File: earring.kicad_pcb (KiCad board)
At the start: 2 copper layers, 41.4 x 41.9 mm, 107 parts, among them J2 USB_C_Receptacle_USB2.0, Q1 NMOS 20V 0.75A 500mΩ@4.5V, Q2 NMOS 20V 0.75A 500mΩ@4.5V, Q3 NMOS 20V 0.75A 500mΩ@4.5V, Q4 NMOS 20V 0.75A 500mΩ@4.5V, Q5 light_sensor, U1 Magnetic Switch, U10 USBLC6-2P6, U20 LGS4056H, U24 SK9822-EC20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

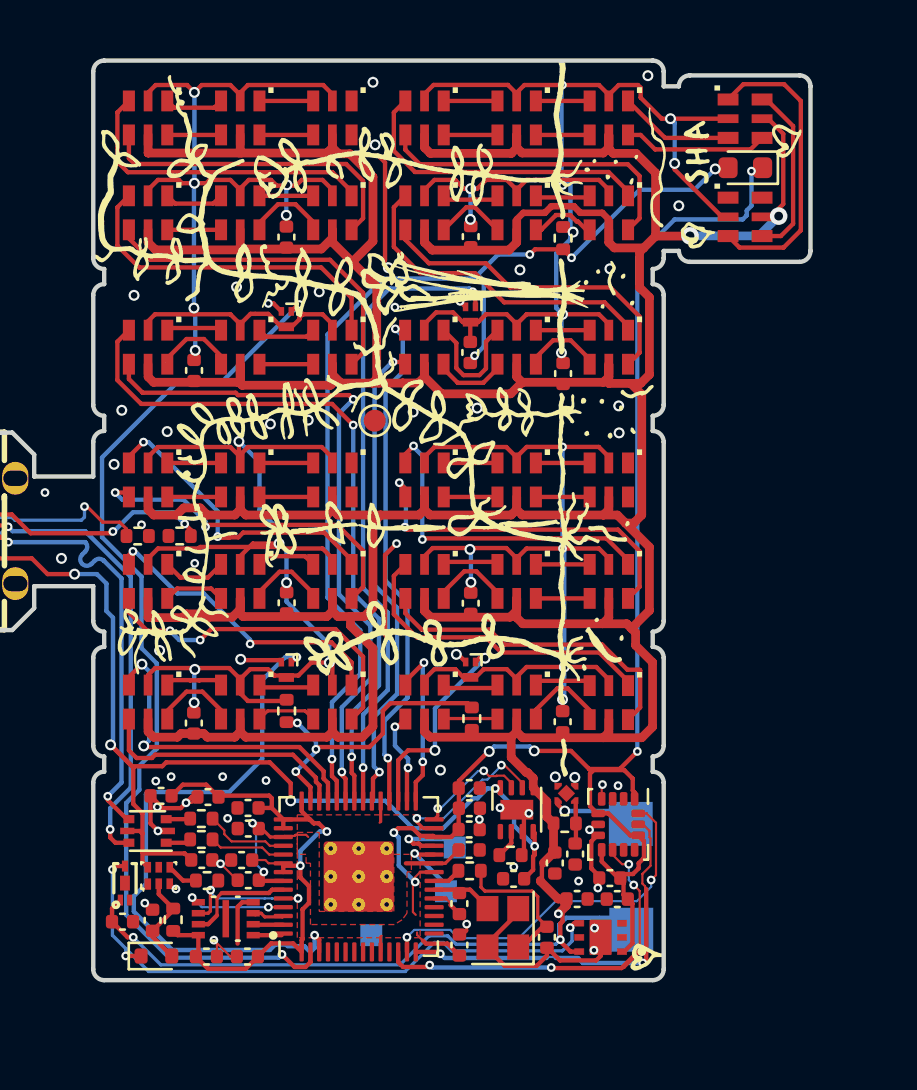
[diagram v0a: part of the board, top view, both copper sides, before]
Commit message: rework power control to simplify and remove VBAT from MCU pins
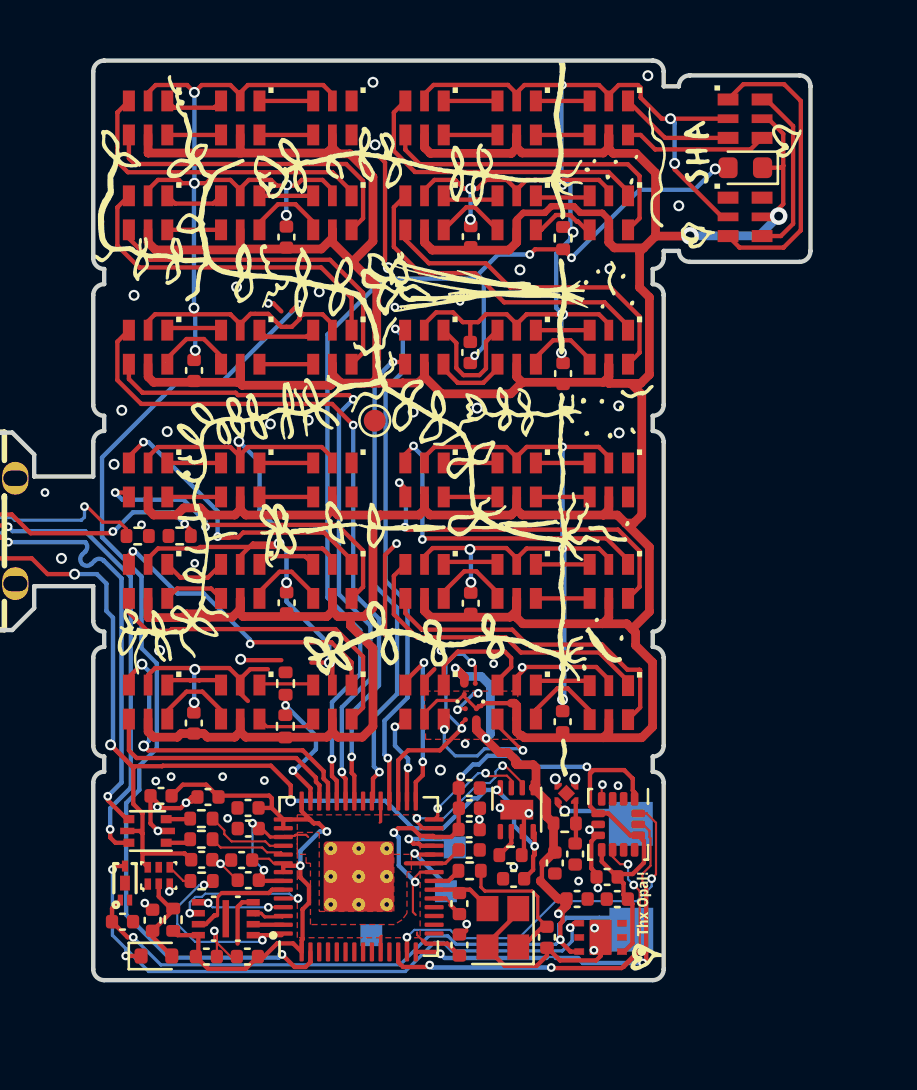
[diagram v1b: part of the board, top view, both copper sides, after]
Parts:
- removed Q1, Q2, Q3, Q4: NMOS 20V 0.75A 500mΩ@4.5V, Package_DFN_QFN:Diodes_DFN1006-3
- added U43: TPS22913BYZVR, footprints:YZV0004ADAD, F.Cu at (167.2, 92.8)
- added U44: TPS22913BYZVR, footprints:YZV0004ADAD, F.Cu at (167.2, 91.6)
- R10: value 20k -> 10k
- U4: value W25Q16JV -> W25Q16JVUXIQ
- U8: value ~ -> DS6091AED4
- moved R11 8.51 mm to (158.8, 93.4)
- moved R12 1.25 mm to (158.8, 91.4)
- moved R1 0.25 mm to (154.9, 100.4)
- moved C23 0.13 mm to (173.4, 100.2)
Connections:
- net /RUN renamed /3v3EN
- C25 pad 1: +BATT -> /LED_1_V
- C25 pad 2: /LED_4_GND -> GND
- C26 pad 1: +BATT -> /LED_1_V
- C26 pad 2: /LED_4_GND -> GND
- C27 pad 1: +BATT -> /LED_1_V
- C27 pad 2: /LED_1_GND -> GND
- C28 pad 1: +BATT -> /LED_1_V
- C28 pad 2: /LED_1_GND -> GND
- C29 pad 1: +BATT -> /LED_1_V
- C29 pad 2: /LED_3_GND -> GND
- C30 pad 1: +BATT -> /LED_1_V
- C30 pad 2: /LED_3_GND -> GND
- C31 pad 1: +BATT -> /LED_1_V
- C31 pad 2: /LED_2_GND -> GND
- C32 pad 1: +BATT -> /LED_1_V
- C32 pad 2: /LED_2_GND -> GND
- C33 pad 2: /LED_2_GND -> GND
- Q5 pad 1: +3V3 -> /LED_1_V
- R1 pad 1: /QSPI_SCLK -> /QSPI_SS
- R11 pad 2: +BATT -> /LED_1_V
- R12 pad 1: /LED_4_GND -> GND
- R8 pad 2: /LED_2_GND -> GND
- U11 pad 2: /LED_4_GND -> GND
- U11 pad 5: +BATT -> /LED_1_V
- U12 pad 2: /LED_4_GND -> GND
- U12 pad 5: +BATT -> /LED_1_V
- U13 pad 2: /LED_4_GND -> GND
- U13 pad 5: +BATT -> /LED_1_V
- U14 pad 2: /LED_4_GND -> GND
- U14 pad 5: +BATT -> /LED_1_V
- U15 pad 2: /LED_4_GND -> GND
- U15 pad 5: +BATT -> /LED_1_V
- U16 pad 2: /LED_1_GND -> GND
- U16 pad 5: +BATT -> /LED_1_V
- U17 pad 2: /LED_1_GND -> GND
- U17 pad 5: +BATT -> /LED_1_V
- U18 pad 2: /LED_1_GND -> GND
- U18 pad 5: +BATT -> /LED_1_V
- U19 pad 2: /LED_1_GND -> GND
- U19 pad 5: +BATT -> /LED_1_V
- U21 pad 2: /LED_1_GND -> GND
- U21 pad 5: +BATT -> /LED_1_V
- U22 pad 2: /LED_1_GND -> GND
- U22 pad 5: +BATT -> /LED_1_V
- U24 pad 2: /LED_3_GND -> GND
- U24 pad 5: +BATT -> /LED_1_V
- U25 pad 2: /LED_3_GND -> GND
- U25 pad 5: +BATT -> /LED_1_V
- U26 pad 2: /LED_3_GND -> GND
- U26 pad 5: +BATT -> /LED_1_V
- U27 pad 2: /LED_2_GND -> GND
- U27 pad 5: +BATT -> /LED_1_V
- U28 pad 2: /LED_2_GND -> GND
- U28 pad 5: +BATT -> /LED_1_V
- U29 pad 2: /LED_2_GND -> GND
- U29 pad 5: +BATT -> /LED_1_V
- U30 pad 2: /LED_2_GND -> GND
- U30 pad 5: +BATT -> /LED_1_V
- U31 pad 2: /LED_3_GND -> GND
- U31 pad 5: +BATT -> /LED_1_V
- U32 pad 2: /LED_3_GND -> GND
- U32 pad 5: +BATT -> /LED_1_V
- U33 pad 2: /LED_3_GND -> GND
- U33 pad 5: +BATT -> /LED_1_V
- U34 pad 2: /LED_2_GND -> GND
- U34 pad 5: +BATT -> /LED_1_V
- U35 pad 2: /LED_2_GND -> GND
- U35 pad 5: +BATT -> /LED_1_V
- U36 pad 2: /LED_2_GND -> GND
- U36 pad 5: +BATT -> /LED_1_V
- U37 pad 2: /LED_2_GND -> GND
- U37 pad 5: +BATT -> /LED_1_V
- U38 pad 2: /LED_3_GND -> GND
- U38 pad 5: +BATT -> /LED_1_V
- U39 pad 2: /LED_3_GND -> GND
- U39 pad 5: +BATT -> /LED_1_V
- U40 pad 2: /LED_3_GND -> GND
- U40 pad 5: +BATT -> /LED_1_V
- U41 pad 2: /LED_2_GND -> GND
- U41 pad 5: +BATT -> /LED_1_V
- U42 pad 2: /LED_2_GND -> GND
- U42 pad 5: +BATT -> /LED_1_V
- U45 pad 2: /LED_4_GND -> GND
- U45 pad 5: +BATT -> /LED_1_V
- U46 pad 2: /LED_4_GND -> GND
- U46 pad 5: +BATT -> /LED_1_V
- U47 pad 2: /LED_4_GND -> GND
- U47 pad 5: +BATT -> /LED_1_V
- U48 pad 2: /LED_1_GND -> GND
- U48 pad 5: +BATT -> /LED_1_V
- U49 pad 2: /LED_1_GND -> GND
- U49 pad 5: +BATT -> /LED_1_V
- U5 pad 2: /LED_4_GND -> GND
- U5 pad 5: +BATT -> /LED_1_V
- U50 pad 2: /LED_2_GND -> GND
- U50 pad 5: +BATT -> /LED_1_V
- U52 pad 2: /LED_1_GND -> GND
- U52 pad 5: +BATT -> /LED_1_V
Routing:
- net /LED_1_V: track 0.00 -> 224.6 mm, vias 0 -> 2
- net +BATT: track 266.3 -> 51.8 mm
- net GND: track 47.9 -> 242.6 mm, vias 61 -> 93
- net /LED_2_GND: track 59.8 -> 0.00 mm, vias 9 -> 0
- net /LED_4_GND: track 50.2 -> 0.00 mm, vias 6 -> 0
- net /LED_3_GND: track 46.3 -> 0.00 mm, vias 6 -> 0
- net /LED_1_GND: track 45.1 -> 0.00 mm, vias 6 -> 0
- net +3V3: track 99.1 -> 66.1 mm, vias 8 -> 6
- net /SW_LED_2: track 29.4 -> 0.00 mm, vias 2 -> 0
- net /SW_LED_4: track 28.2 -> 0.00 mm, vias 2 -> 0
- net /BATT_SENSE: track 13.7 -> 6.68 mm, vias 3 -> 2
- net /QSPI_SS: track 1.40 -> 8.06 mm, vias 0 -> 2
- net Net-(U48-CKO): track 2.47 -> 7.07 mm, vias 0 -> 2
- net Net-(U48-SDO): track 2.56 -> 6.22 mm
- net /SW_LED_1: track 9.38 -> 11.6 mm
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- added copper zone on F.Cu, net /LED_1_V
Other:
- board text added: "Thx Opal!"

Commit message: check in complex startup circuit before simplification
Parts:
- removed C24: 100n, Capacitor_SMD:C_0402_1005Metric
- removed R2: 100k, Resistor_SMD:R_0402_1005Metric
- removed U6: Buffer, digikey-footprints:UFDFN-6_1.45x1mm
- added D1: D, Diode_SMD:D_SOD-882, F.Cu at (136.0, 104.1)
- added D3: 3.3v Zener, Diode_SMD:D_SOD-882, F.Cu at (143.5, 106.0)
- added D4: D, Diode_SMD:D_SOD-882, F.Cu at (147.5, 100.6)
- added D5: D, Diode_SMD:D_SOD-882, F.Cu at (136.2, 101.3)
- added Q1: BSS214NW, Package_DFN_QFN:Diodes_DFN1006-3, F.Cu at (147.5, 102.9)
- added Q2: BSS214NW, Package_DFN_QFN:Diodes_DFN1006-3, F.Cu at (142.9, 99.4)
- added R13: 100k, Resistor_SMD:R_0402_1005Metric, F.Cu at (143.8, 101.8)
- added R15: 100k, Resistor_SMD:R_0402_1005Metric, F.Cu at (139.2, 103.9)
- added R16: 100k, Resistor_SMD:R_0402_1005Metric, F.Cu at (139.9, 99.0)
- added R17: 1M, Resistor_SMD:R_0402_1005Metric, F.Cu at (139.9, 101.0)
- added R18: 10k, Resistor_SMD:R_0402_1005Metric, F.Cu at (145.8, 105.6)
- added R20: 10k, Resistor_SMD:R_0402_1005Metric, F.Cu at (143.7, 104.4)
- D2: value D -> 3.3v Zener; footprint Diode_SMD:D_SOD-523 -> Diode_SMD:D_SOD-882
- moved C3 14.0 mm to (139.2, 105.9), turned to 0 degrees
- moved D2 7.75 mm to (147.5, 98.3)
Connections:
- C3 pad 1: Net-(D2-A) -> /~{USB_BOOT}
- C3 pad 2: GND -> Net-(Q2-D)
- D2 pad 1: /3v3EN -> /RUN
- D2 pad 2: Net-(D2-A) -> GND
- U1 pad 2: /3v3EN -> /mag
- U3 pad 2: /SW_LED_3 -> /ENA_GPIO
- U3 pad 26: +3V3 -> /RUN
- U3 pad 3: /SW_LED_4 -> /RUN
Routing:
- net /SW_LED_3: track 44.9 -> 0.00 mm, vias 2 -> 0
- net /ENA_GPIO: track 0.00 -> 44.9 mm, vias 0 -> 2
- net Net-(D2-A): track 4.59 -> 0.00 mm
- net +3V3: track 66.1 -> 63.9 mm
- net /~{USB_BOOT}: track 1.20 -> 0.32 mm
- net VBUS: track 57.8 -> 57.0 mm
- net /QSPI_SS: track 8.06 -> 7.29 mm
- net GND: track 242.6 -> 242.2 mm, vias 93 -> 91

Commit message: simplify power and boot circuit
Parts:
- removed C3: 10u, Capacitor_SMD:C_0402_1005Metric
- removed D2, D3: 3.3v Zener, Diode_SMD:D_SOD-882
- removed D5: D, Diode_SMD:D_SOD-882
- removed Q1, Q2: BSS214NW, Package_DFN_QFN:Diodes_DFN1006-3
- removed R15, R16: 100k, Resistor_SMD:R_0402_1005Metric
- removed R17: 1M, Resistor_SMD:R_0402_1005Metric
- removed R18, R20: 10k, Resistor_SMD:R_0402_1005Metric
- added TP7: TestPoint, TestPoint:TestPoint_Pad_D1.0mm, B.Cu at (153.8, 100.3)
- added TP8: TestPoint, TestPoint:TestPoint_Pad_D1.0mm, B.Cu at (154.9, 97.3)
- moved D1 17.3 mm to (153.2, 102.3)
- moved R13 9.36 mm to (152.9, 99.7)
- moved D4 5.41 mm to (152.9, 100.9)
- moved R1 0.07 mm to (155.0, 100.4)
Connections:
- D1 pad 1: /RUN -> /3v3EN
- D1 pad 2: /~{USB_BOOT} -> VBUS
- D4 pad 1: Net-(D3-K) -> /3v3EN
- D4 pad 2: VBUS -> Net-(D4-A)
- R13 pad 1: +BATT -> Net-(U1-VOUT)
- R13 pad 2: /3v3EN -> Net-(D4-A)
- U1 pad 2: /mag -> Net-(U1-VOUT)
- U3 pad 26: /RUN -> +3V3
- U3 pad 3: /RUN -> /RUN_GPIO
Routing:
- net /3v3EN: track 28.3 -> 25.5 mm, vias 3 -> 2
- net VBUS: track 57.0 -> 59.6 mm
- net /~{USB_BOOT}: track 0.32 -> 1.87 mm, vias 0 -> 1
- net /QSPI_SS: track 7.29 -> 8.61 mm
- net Net-(D4-A): track 0.00 -> 1.21 mm
- net Net-(U1-VOUT): track 0.00 -> 0.98 mm
- net +3V3: track 63.9 -> 64.7 mm
- net GND: vias 91 -> 93
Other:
- board text added: "Thanks Stardust"
- board text removed: "Thx Opal!"

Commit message: pcb files seem possibly ready to order
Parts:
- moved TP8 1.04 mm to (154.6, 98.3)
- moved D4 0.06 mm to (152.9, 100.9)
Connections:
- U3 pad 2: /ENA_GPIO -> unconnected-(U3-GPIO0-Pad2)
- U3 pad 3: /RUN_GPIO -> unconnected-(U3-GPIO1-Pad3)
- U3 pad 35: /SW_LED_2 -> unconnected-(U3-GPIO23-Pad35)
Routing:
- net /ENA_GPIO: track 44.9 -> 0.00 mm, vias 2 -> 0
- net Net-(U15-CKO): track 15.7 -> 17.1 mm
- net Net-(U16-CKL): track 16.5 -> 15.4 mm
- net /BATT_SENSE: track 6.68 -> 5.87 mm
- net /QSPI_SS: track 8.61 -> 7.86 mm
- net Net-(U16-SDI): track 15.4 -> 14.7 mm
- net Net-(U15-SDO): track 14.0 -> 14.6 mm
- net GND: track 242.2 -> 241.9 mm, vias 93 -> 95
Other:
- board text added: "Boot"
- board text added: "u inspire me"
- board text removed: "Thanks Stardust"

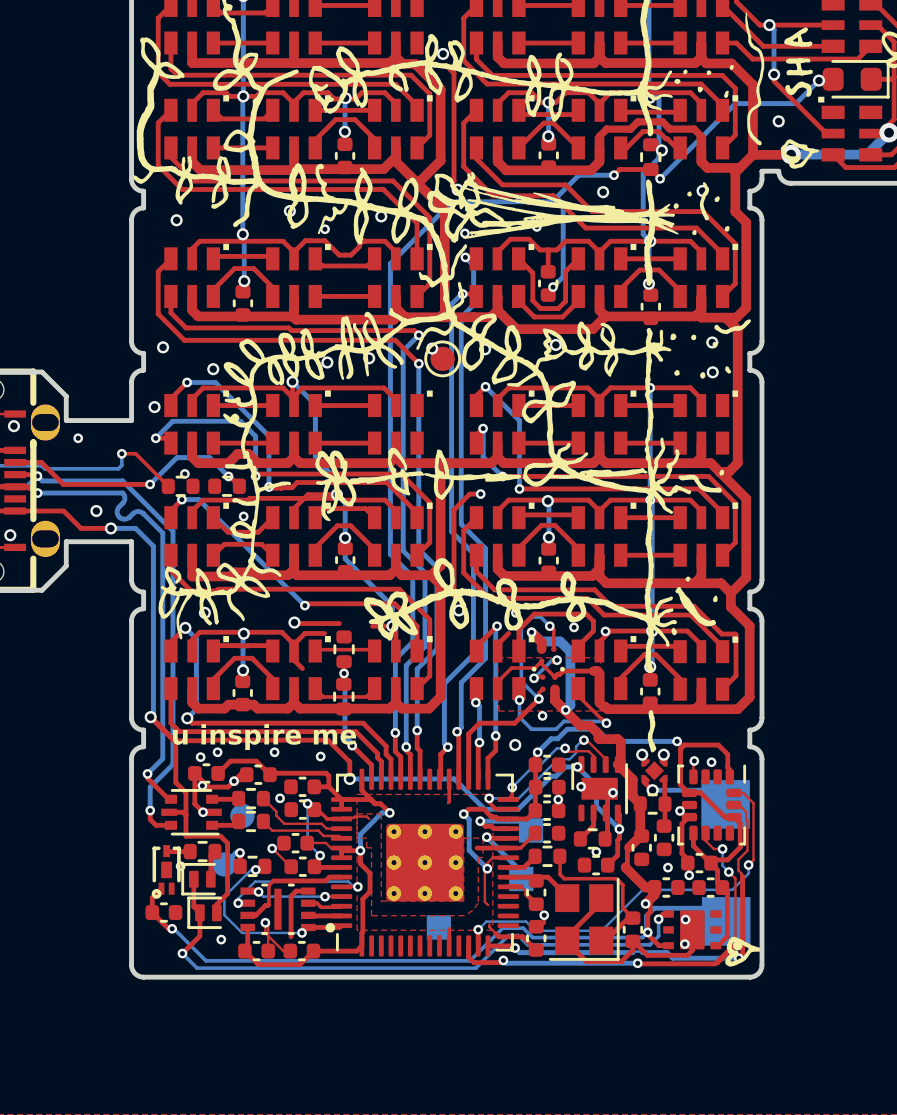
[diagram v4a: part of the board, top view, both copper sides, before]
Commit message: Fixed power circuit and ordered June 2025
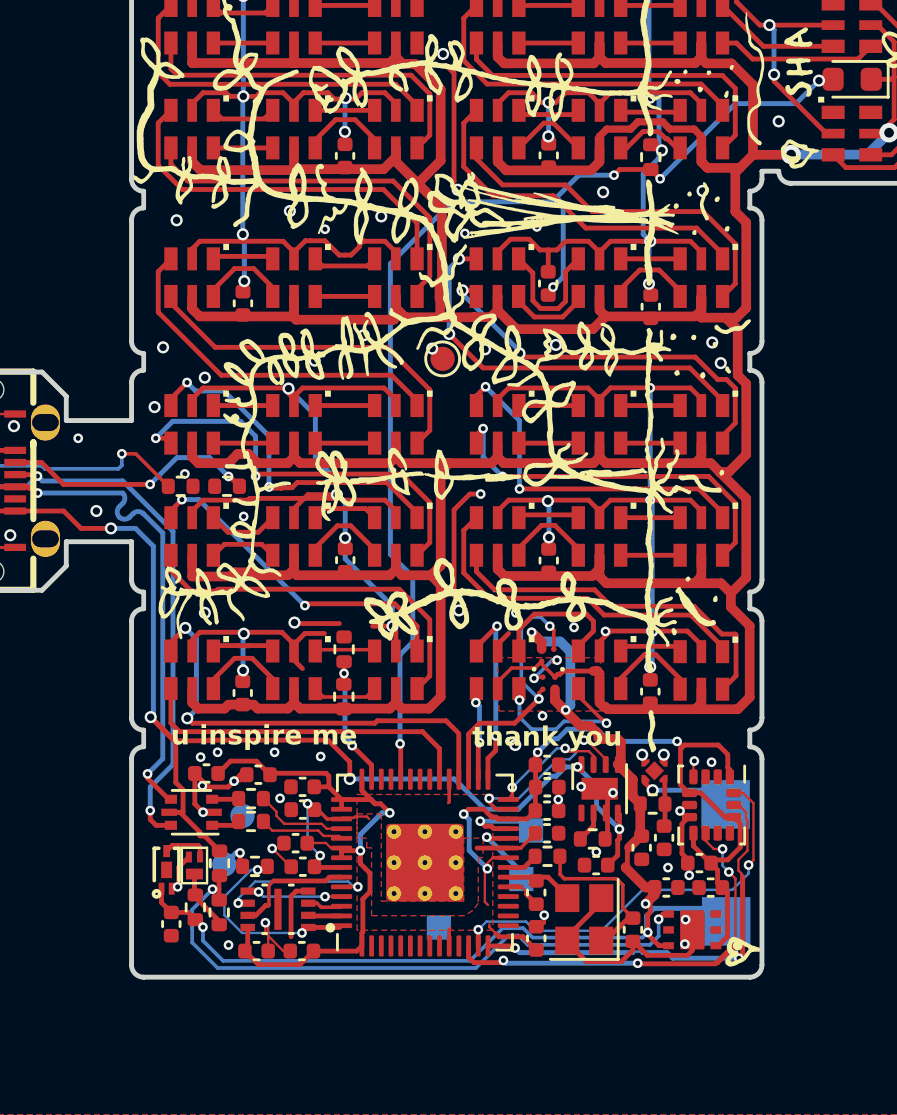
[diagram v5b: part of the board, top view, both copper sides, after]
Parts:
- removed D1, D4: D, Diode_SMD:D_SOD-882
- added Q1: Q_NMOS_SGD, parts2:DFN1006-3L_L1.0-W0.6-BL, F.Cu at (152.6, 100.3)
- added R15: 10k, Resistor_SMD:R_0402_1005Metric, F.Cu at (153.6, 102.3)
- added R2: 10k, Resistor_SMD:R_0402_1005Metric, F.Cu at (153.6, 100.2)
- C4: value 100n -> 10u
- C5, C6: value 20p -> 12p
- U24: value SK9822-EC20 -> ~
- moved R13 2.32 mm to (152.6, 102.0), turned to -90 degrees
- moved C19 0.56 mm to (151.6, 102.7), turned to -90 degrees
- moved R1 0.10 mm to (155.1, 100.4)
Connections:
- R13 pad 1: Net-(U1-VOUT) -> Net-(Q1-D)
- R13 pad 2: Net-(D4-A) -> +BATT
- U1 pad 2: Net-(U1-VOUT) -> Net-(Q1-G)
- U12 pad 1: unconnected-(U12-SDO-Pad1) -> Net-(U12-SDO)
- U12 pad 6: unconnected-(U12-CKO-Pad6) -> Net-(U12-CKO)
- U18 pad 1: unconnected-(U18-SDO-Pad1) -> Net-(U18-SDO)
- U18 pad 6: unconnected-(U18-CKO-Pad6) -> Net-(U18-CKO)
- U20 pad 6: /CHRG -> /DONE
- U20 pad 7: /DONE -> /CHRG
- U3 pad 27: /CHRG -> /DONE
- U3 pad 28: /DONE -> /CHRG
- U3 pad 36: /LED_TX_3 -> unconnected-(U3-GPIO24-Pad36)
- U3 pad 37: /LED_SCK_3 -> unconnected-(U3-GPIO25-Pad37)
- U3 pad 39: /LED_TX_4 -> unconnected-(U3-GPIO27_ADC1-Pad39)
- U3 pad 40: /LED_SCK_4 -> unconnected-(U3-GPIO28_ADC2-Pad40)
- U38 pad 3: /LED_TX_3 -> Net-(U12-SDO)
- U38 pad 4: /LED_SCK_3 -> Net-(U12-CKO)
- U41 pad 3: /LED_TX_2 -> Net-(U18-SDO)
- U41 pad 4: /LED_SCK_2 -> Net-(U18-CKO)
- U45 pad 3: /LED_TX_4 -> /LED_TX_2
- U45 pad 4: /LED_SCK_4 -> /LED_SCK_2
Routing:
- net /LED_TX_3: track 31.9 -> 0.00 mm, vias 2 -> 0
- net /LED_SCK_3: track 30.6 -> 0.00 mm, vias 2 -> 0
- net Net-(U18-SDO): track 0.00 -> 16.6 mm, vias 0 -> 2
- net Net-(U18-CKO): track 0.00 -> 16.2 mm, vias 0 -> 2
- net /LED_TX_4: track 15.4 -> 0.00 mm, vias 2 -> 0
- net Net-(U12-CKO): track 0.00 -> 14.8 mm
- net Net-(U12-SDO): track 0.00 -> 14.8 mm
- net /LED_SCK_4: track 11.6 -> 0.00 mm
- net /LED_SCK_2: track 21.9 -> 14.2 mm, vias 2 -> 0
- net /LED_TX_2: track 23.3 -> 18.6 mm
- net VBUS: track 59.6 -> 55.9 mm
- net Net-(Q1-D): track 0.00 -> 2.52 mm
- net /DONE: track 5.09 -> 7.57 mm
- net /CHRG: track 7.57 -> 5.09 mm
- net Net-(Q1-G): track 0.00 -> 1.91 mm
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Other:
- board text added: "thank you"
